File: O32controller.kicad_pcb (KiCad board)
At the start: 4 copper layers, 27 x 27 mm, 58 parts, among them J1 Conn_01x08_MountingPin, J2 BATT+, J3 BATT-, J4 Motor Connection, J5 Motor Connection, J6 Motor Connection, J7 BATT+, J8 BATT-, Q1 CSD88584Q5DCT, Q2 CSD88584Q5DCT, Q3 CSD88584Q5DCT, U1 AS5047D, U2 STSPIN32F0A

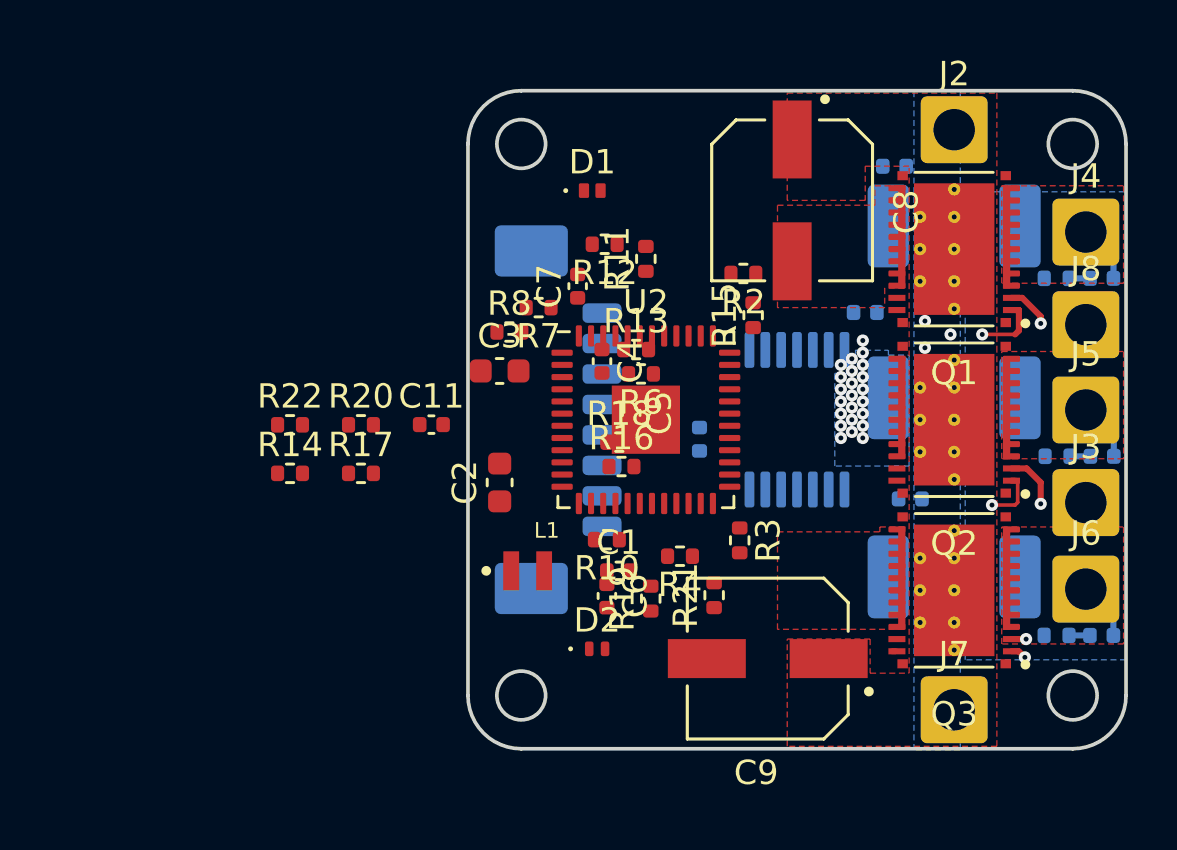
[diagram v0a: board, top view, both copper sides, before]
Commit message: routed some sense, netties, fixed NC
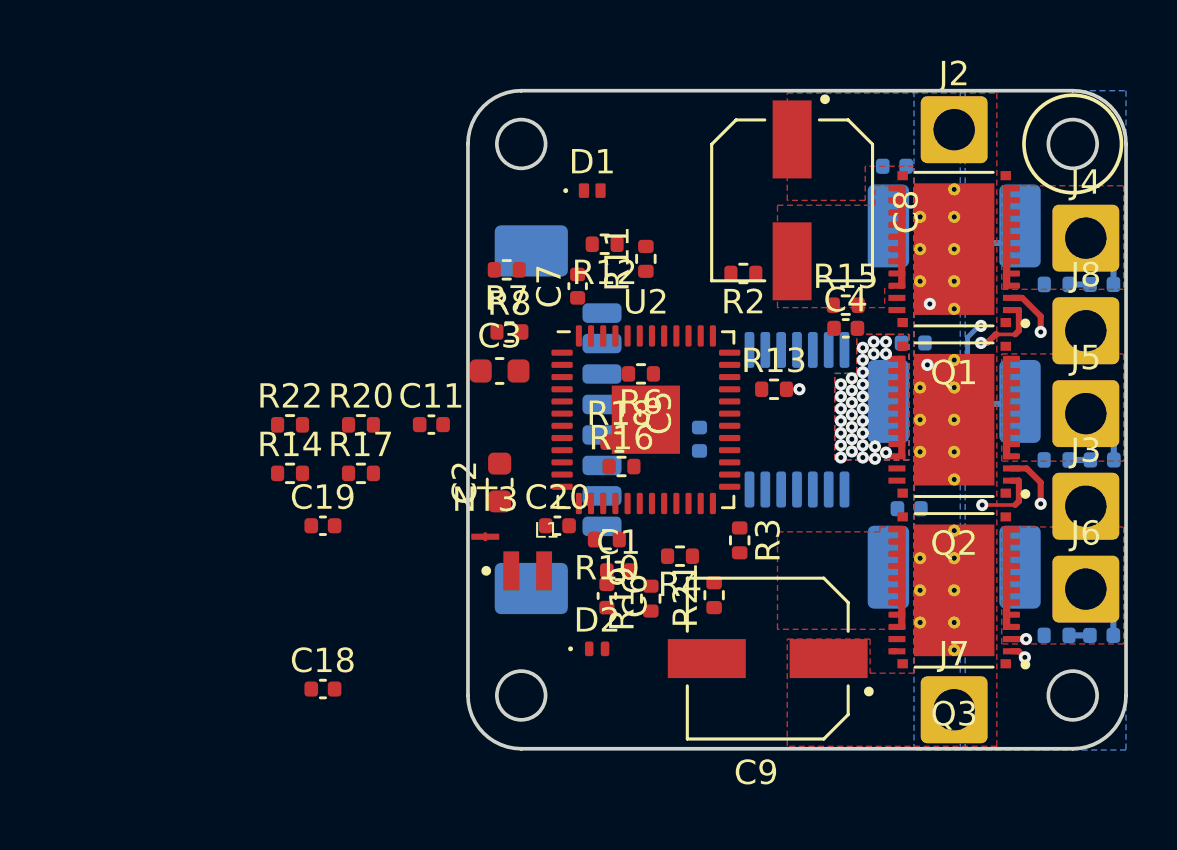
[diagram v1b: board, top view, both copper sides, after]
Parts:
- added C18: 1nF, Capacitor_SMD:C_0402_1005Metric, F.Cu at (30.6, 61.0)
- added C19: 1nF, Capacitor_SMD:C_0402_1005Metric, F.Cu at (30.6, 54.4)
- added C20: 1nF, Capacitor_SMD:C_0402_1005Metric, F.Cu at (40.2, 54.4)
- added NT1: Sense_N, NetTie:NetTie-small, B.Cu at (57.9, 42.8)
- added NT2: Sense_N, NetTie:NetTie-small, B.Cu at (57.8, 49.4)
- added NT3: Sense_N, NetTie:NetTie-small, F.Cu at (37.2, 54.8)
- moved C4 10.1 mm to (52.0, 46.2), turned to 0 degrees
- moved R13 5.89 mm to (49.1, 48.8)
- moved R15 3.82 mm to (52.0, 45.3), turned to 0 degrees
- moved C14 2.33 mm to (54.8, 46.9)
- moved R7 2.03 mm to (38.1, 43.9)
- moved C16 0.40 mm to (54.6, 53.6)
- moved R9 0.40 mm to (56.5, 56.0)
- moved C13 0.25 mm to (62.5, 44.5)
- moved J4 0.25 mm to (61.9, 42.5)
- moved J8 0.25 mm to (61.9, 46.4)
- moved R23 0.25 mm to (60.7, 44.5)
- moved R24 0.16 mm to (60.6, 51.6)
- moved C15 0.15 mm to (62.5, 51.6)
- moved J3 0.15 mm to (61.9, 53.5)
- moved J5 0.15 mm to (61.9, 49.8)
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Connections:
- net /Motor phase U/Motor renamed Net-(C13-Pad1)
- net /Motor phase V/Motor renamed Net-(C15-Pad1)
- net /Motor phase W/Motor renamed Net-(C17-Pad1)
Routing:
- net /Motor phase V/Sense_N: track 0.00 -> 7.77 mm, vias 0 -> 1
- net /OUTU: track 1.81 -> 9.02 mm
- net /Motor phase U/GH_MOS: track 2.72 -> 7.21 mm, vias 1 -> 2
- net unconnected-(U1-Pad14): vias 3 -> 0
- net VBUS: vias 3 -> 2
- net /Motor phase V/Sense_P: vias 20 -> 31
- added copper zone on F.Cu, net /Motor phase V/Sense_P
- removed copper zone on In1.Cu, net GND
- removed copper zone on In2.Cu, net GND

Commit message: routed most of power stage, no drc violations
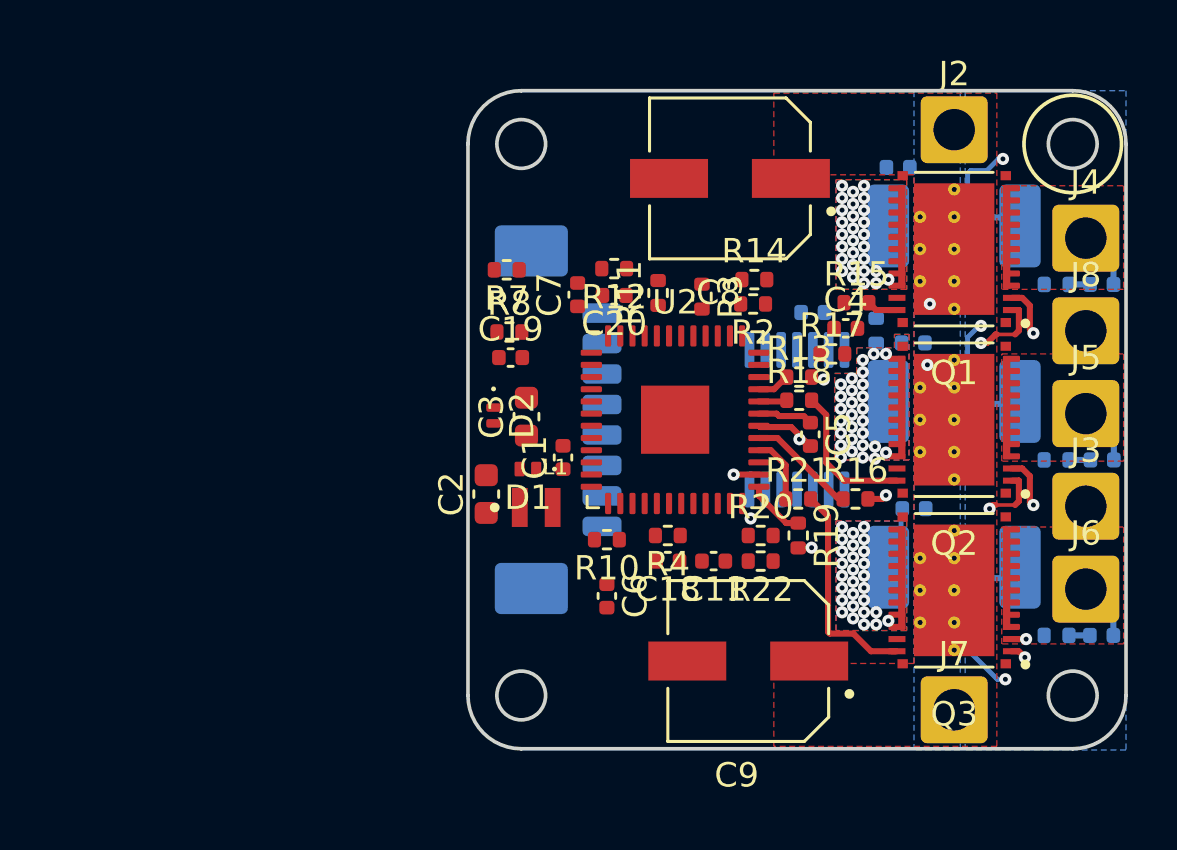
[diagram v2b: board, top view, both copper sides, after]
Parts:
- NT3, R6: moved to B.Cu
- moved NT3 20.7 mm to (57.9, 56.5)
- moved R14 20.6 mm to (48.2, 44.2)
- moved R22 20.1 mm to (48.5, 55.8), turned to 180 degrees
- moved R17 20.0 mm to (51.5, 47.3)
- moved R20 17.0 mm to (48.5, 54.8)
- moved C18 15.1 mm to (44.7, 55.8), turned to 180 degrees
- moved C11 12.9 mm to (46.6, 55.8), turned to 180 degrees
- moved D1 11.7 mm to (39.0, 52.0), turned to 180 degrees
- moved D2 10.5 mm to (37.5, 49.8), turned to -90 degrees
- moved C19 10.3 mm to (38.2, 47.5)
- moved R3 10.1 mm to (46.1, 45.0)
- moved R6 9.81 mm to (53.2, 46.4), turned to 90 degrees
- moved C20 9.73 mm to (42.5, 44.9), turned to 180 degrees
- moved R16 9.69 mm to (52.4, 53.2)
- moved R18 7.58 mm to (50.1, 49.2)
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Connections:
- net Net-(D1-Pad1) renamed /SW_3.3
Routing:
- net /Motor phase W/Sense_N: track 0.00 -> 26.6 mm, vias 0 -> 1
- net /OUTW: track 0.60 -> 17.2 mm, vias 1 -> 2
- net /OUTV: track 2.31 -> 16.0 mm, vias 1 -> 2
- net /Motor phase U/Sense_N: track 0.00 -> 13.2 mm, vias 0 -> 1
- net /Motor phase W/GH_MOS: track 0.65 -> 13.6 mm, vias 1 -> 2
- net /Motor phase W/GL_MOS: track 0.15 -> 9.05 mm
- net /Motor phase V/GL_MOS: track 0.00 -> 6.02 mm
- net /Motor phase V/GH_MOS: track 2.80 -> 7.84 mm, vias 1 -> 2
- net /HSV: track 0.00 -> 4.47 mm
- net /Motor phase U/GH_MOS: track 7.21 -> 10.1 mm
- net /LSW: track 0.00 -> 2.74 mm
- net /Motor phase W/Sense_P: track 0.00 -> 2.62 mm, vias 0 -> 28
- net /HSW: track 0.00 -> 2.45 mm
- net /VBOOTV: track 0.00 -> 2.27 mm
- net /HSU: track 0.00 -> 1.35 mm
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- added copper zone on B.Cu, net /Motor phase U/Sense_P
- added copper zone on B.Cu, net /Motor phase W/Sense_P

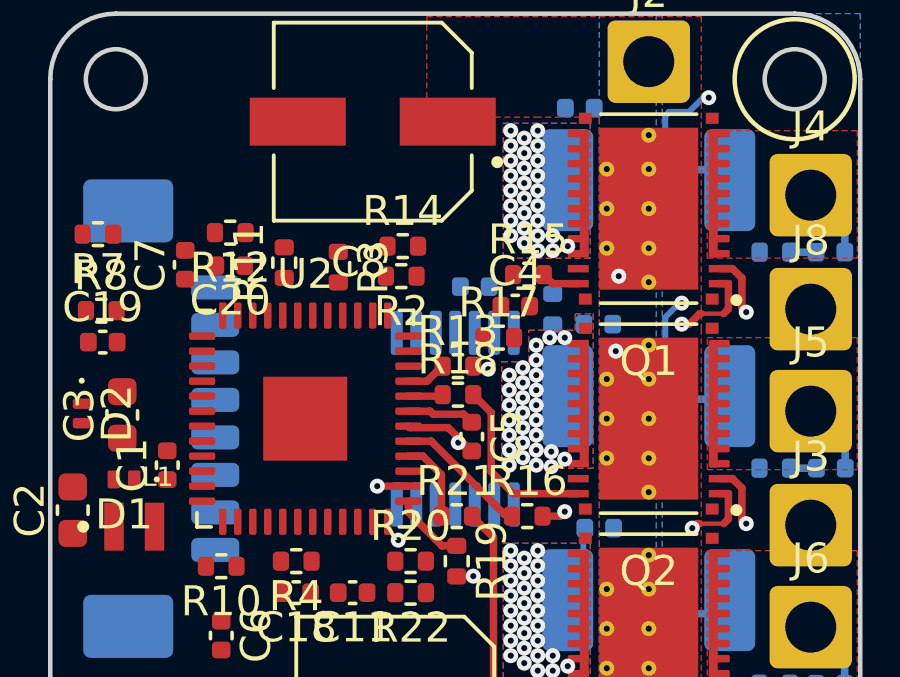
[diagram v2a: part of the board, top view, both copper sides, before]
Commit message: trying to fix shunt footprint:
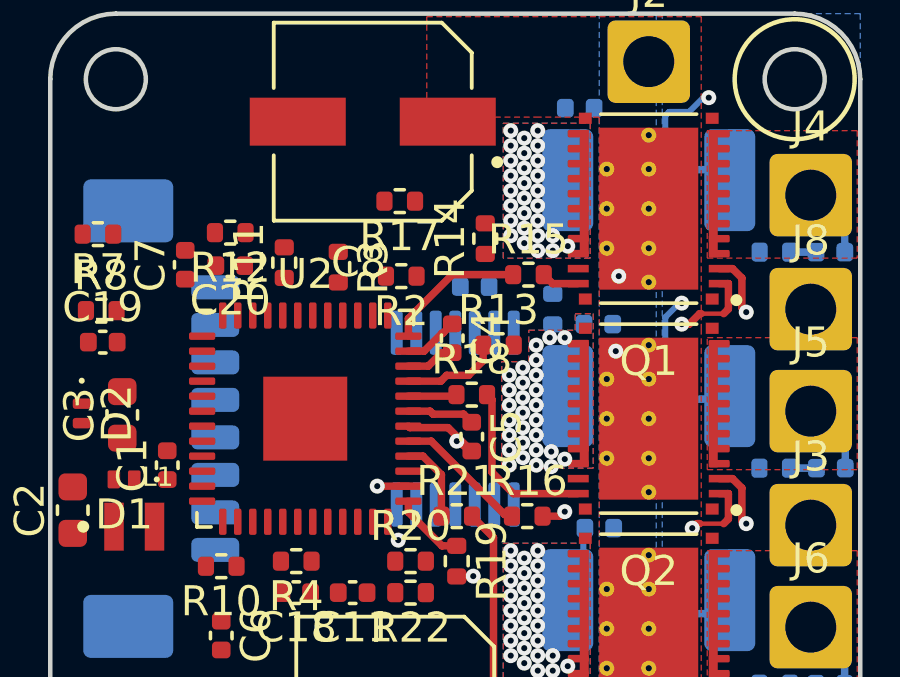
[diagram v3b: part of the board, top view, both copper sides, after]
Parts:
- moved R17 5.62 mm to (48.1, 42.8), turned to 180 degrees
- moved R14 2.76 mm to (51.0, 44.0), turned to 90 degrees
- moved C4 2.36 mm to (49.9, 47.3), turned to -90 degrees
- moved R13 1.52 mm to (51.4, 47.5)
- moved R18 0.46 mm to (50.5, 49.2)
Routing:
- net /LSU: track 0.00 -> 4.69 mm
- net /Motor phase U/GH_MOS: track 10.1 -> 7.80 mm, vias 2 -> 1
- net /HSU: track 1.35 -> 3.29 mm
- net /VBOOTU: track 0.00 -> 1.84 mm
- net /OUTU: track 8.80 -> 10.4 mm

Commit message: fixed clearances
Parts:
- Q1, Q2, Q3: value CSD88584Q5DCT -> DMM0022A
- R1, R5, R9: value WFCP06124L000FE66 0.004R -> WSLF25122L000FEB 0.002R
- turned R15 to 180 degrees
- turned R18 to 180 degrees
- turned R21 to 180 degrees
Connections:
- R15 pad 1: /LSU -> /Motor phase U/GL_MOS
- R15 pad 2: /Motor phase U/GL_MOS -> /LSU
- R18 pad 1: /LSV -> /Motor phase V/GL_MOS
- R18 pad 2: /Motor phase V/GL_MOS -> /LSV
- R21 pad 1: /LSW -> /Motor phase W/GL_MOS
- R21 pad 2: /Motor phase W/GL_MOS -> /LSW

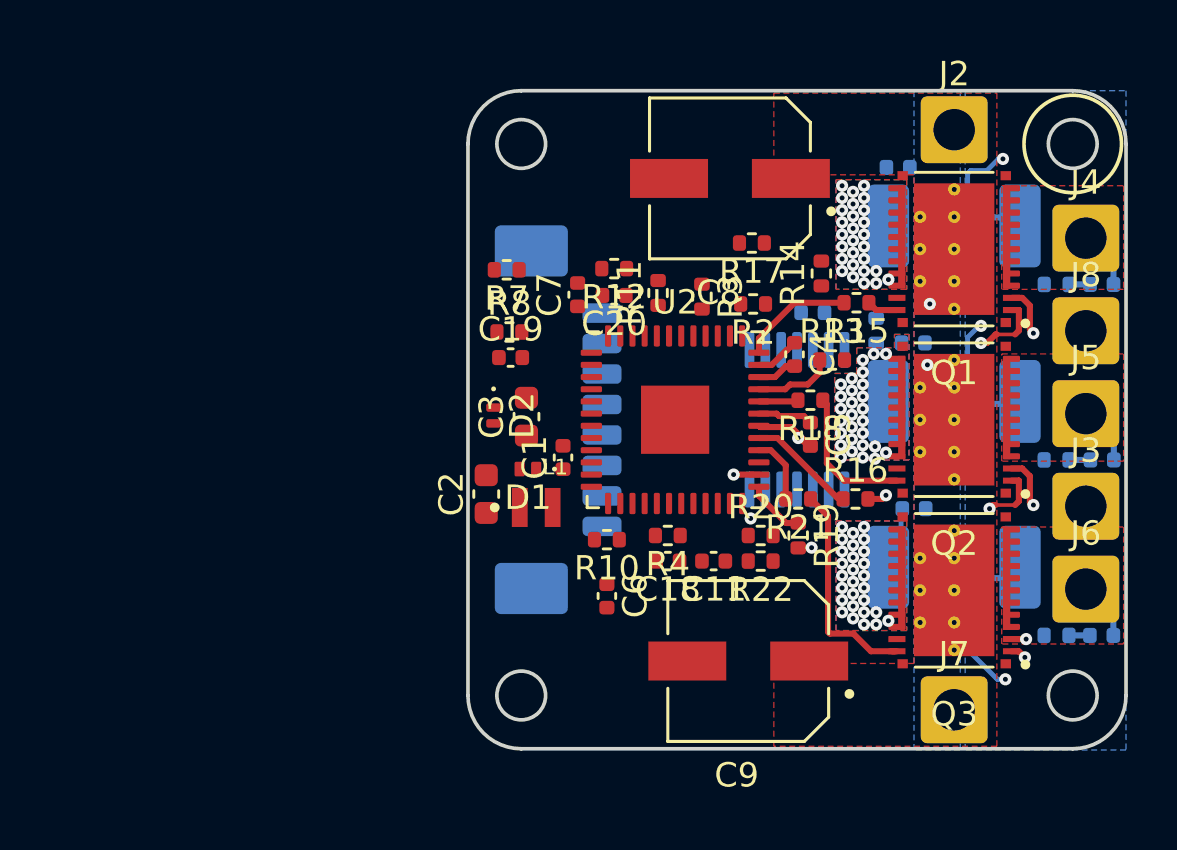
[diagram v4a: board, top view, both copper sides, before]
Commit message: routed more signals
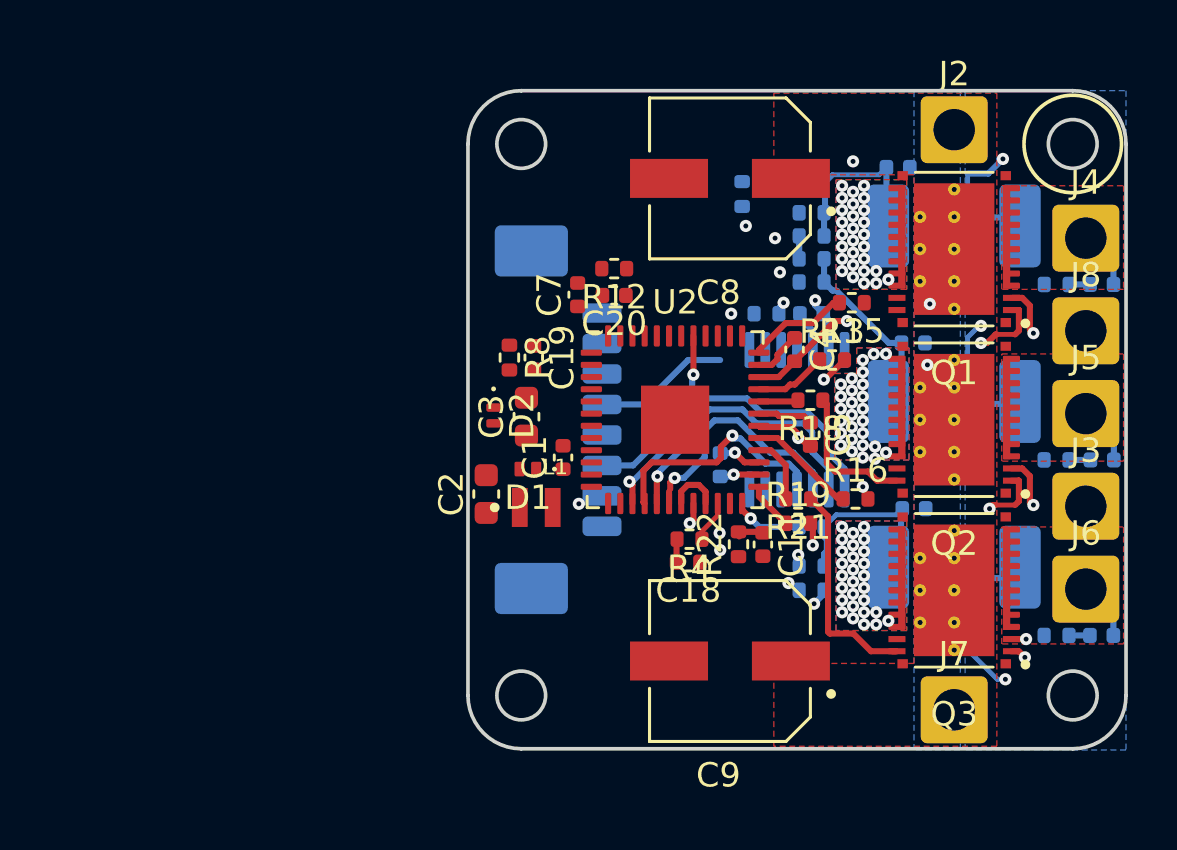
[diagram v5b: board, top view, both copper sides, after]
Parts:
- C6, R10, R11, R14, R17, R2, R20, R3, R7: moved to B.Cu
- moved R11 13.7 mm to (50.6, 57.0), turned to 180 degrees
- moved R7 10.8 mm to (48.8, 45.6)
- moved R10 8.47 mm to (50.6, 56.0)
- moved C6 7.11 mm to (46.9, 51.9)
- moved R3 4.52 mm to (47.8, 40.7)
- moved R2 4.44 mm to (50.6, 41.5)
- moved R6 3.32 mm to (50.6, 44.4), turned to 180 degrees
- moved R17 2.53 mm to (50.6, 43.4), turned to 0 degrees
- moved C11 2.13 mm to (48.6, 55.1), turned to -90 degrees
- moved R20 2.12 mm to (50.6, 54.4)
- moved R14 1.59 mm to (50.6, 42.5), turned to 0 degrees
- moved R22 1.14 mm to (47.6, 55.1), turned to 90 degrees
- moved R8 1.05 mm to (38.2, 47.5), turned to -90 degrees
- moved C19 0.95 mm to (39.2, 47.5), turned to -90 degrees
- moved R4 0.90 mm to (45.6, 54.9)
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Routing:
- net /OC_COMP: track 0.00 -> 16.7 mm, vias 1 -> 2
- net /OP_U_N: track 0.00 -> 16.4 mm, vias 0 -> 2
- net /OP_W_N: track 0.00 -> 15.8 mm, vias 0 -> 1
- net /OP_W_P: track 0.00 -> 14.2 mm, vias 0 -> 1
- net /~{MAG_CS}: track 0.00 -> 14.0 mm, vias 0 -> 1
- net /OP_U_P: track 0.00 -> 13.5 mm, vias 0 -> 2
- net SPI_MISO: track 0.00 -> 12.0 mm, vias 0 -> 1
- net /Motor phase W/Sense_N: track 26.6 -> 15.4 mm, vias 1 -> 2
- net SPI_MOSI: track 0.00 -> 9.90 mm, vias 0 -> 1
- net SPI_SCLK: track 0.00 -> 9.89 mm, vias 0 -> 1
- net /Motor phase V/Sense_P: track 0.05 -> 7.90 mm, vias 28 -> 27
- net I2C_SDA: track 0.00 -> 7.61 mm, vias 0 -> 1
- net /Motor phase U/Sense_P: track 0.00 -> 7.43 mm
- net /Motor phase W/Sense_P: track 2.62 -> 8.28 mm
- net SWD_CLK: track 0.00 -> 5.61 mm
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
